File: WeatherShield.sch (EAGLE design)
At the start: 66 parts, among them J7 M023.5MM, J8 M023.5MM, Q1 BSS138, Q2 BSS138, U1 DS3231SN, U2 LT3652, U4 MPL3115A2LGA8, U5 HTU21D

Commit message: Power parts
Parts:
- removed J7, J8: M023.5MM, SparkFun-Connectors:M023.5MM
- removed L1: 68uH, SparkFun-Passives:INDUCTOR68UH-1A
- added L2: (no value), rcl:L-EU6000-XXX-RC
- C3, C4: device SparkFun-Capacitors:47UF-TANT -> FSEWeatherShield:47UF-16V-10%(TANT)
- R21, R23, R8: device rcl:R-EU_R0603 -> rcl:R-EU_R0805
- U$3: value DEAN_CONNECTOR -> V_BATT
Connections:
- net GND: no longer J8.2
- net N$14: no longer J7.2, J8.1
- net SENSE: now also L2.2; no longer L1.2
- net SFSASDF: no longer J7.1
- net SW: now also L2.1; no longer L1.1
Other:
- note added: "Ichg = .1/(R8) Add more Resitors parallel to increase Ichg"
- note added: "NB: DO NOT short JP1 & JP2 !! With both JP1 and JP2 shorted, the second power input is also shorted! This may result in damage to your power source."
- note removed: "01"
- note removed: "Ichg = .1/(R8) Add more Resitors in parallel to increase Ichg"
- note removed: "NB: With both JP1 and JP2 shorted, the second power input is also shorted! This may result in damage to your power source. You've been warned!"
- moved on the sheet: C9, D1, D3, JP1, JP10-DNP, JP2, JP9-DNP1, JP9-DNP2, R1, R15, R21, R23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

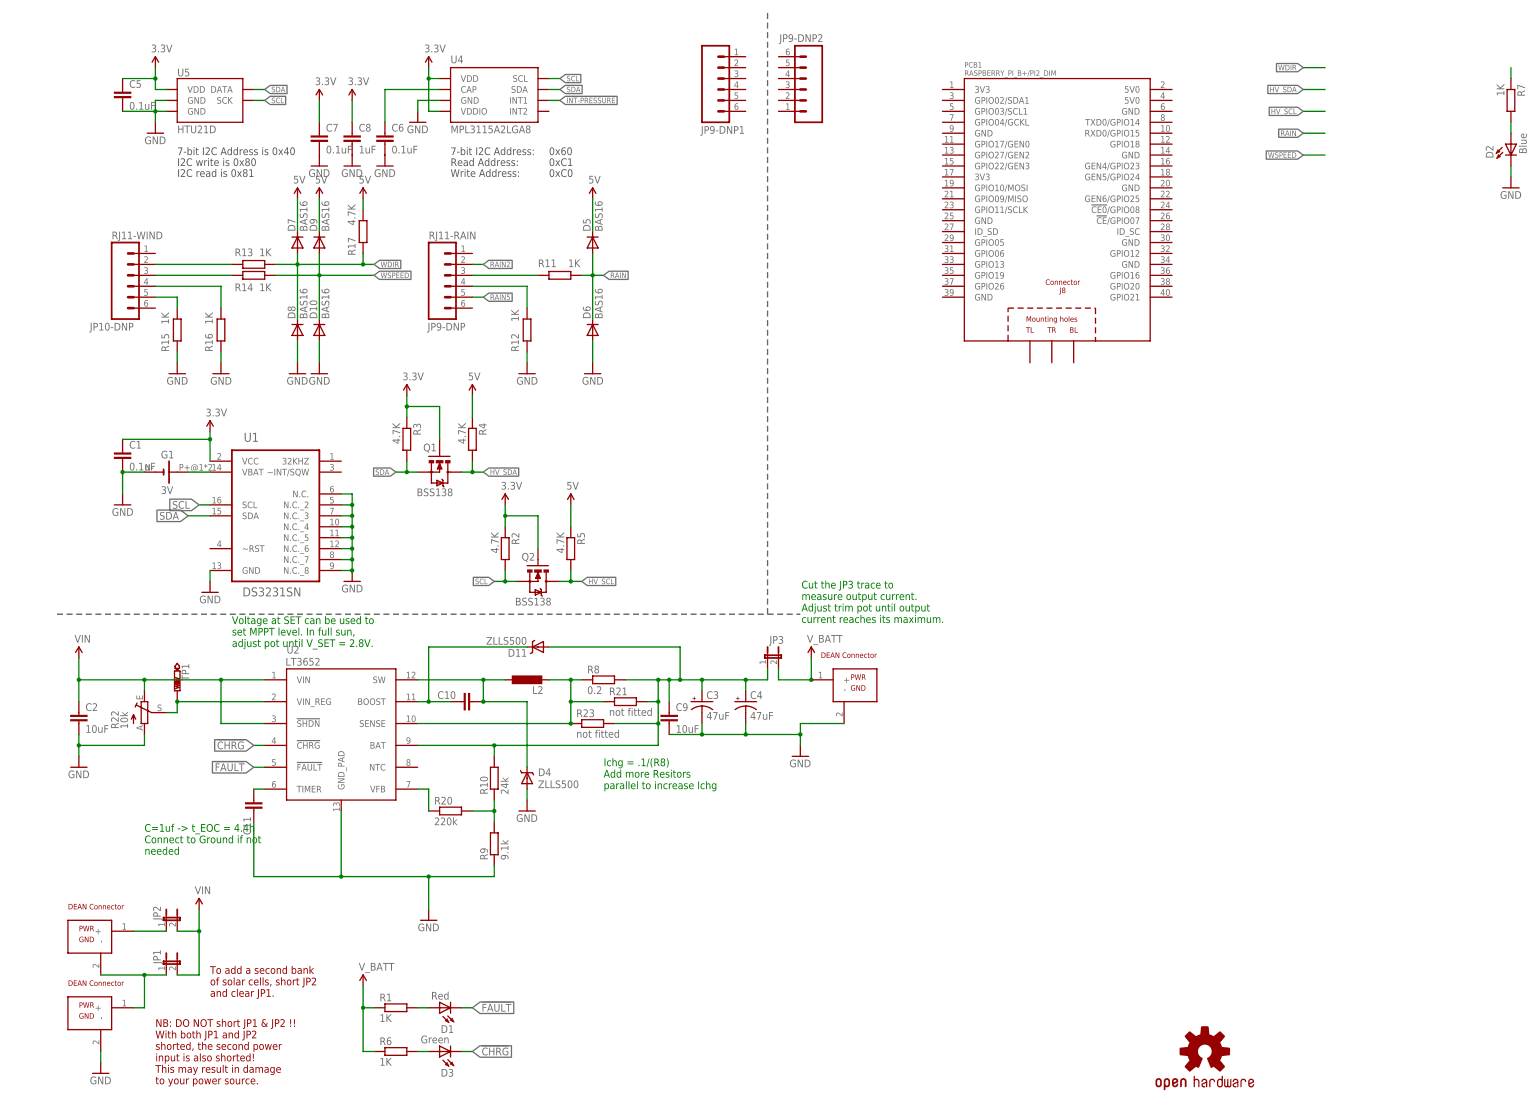
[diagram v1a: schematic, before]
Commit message: 5V supply done
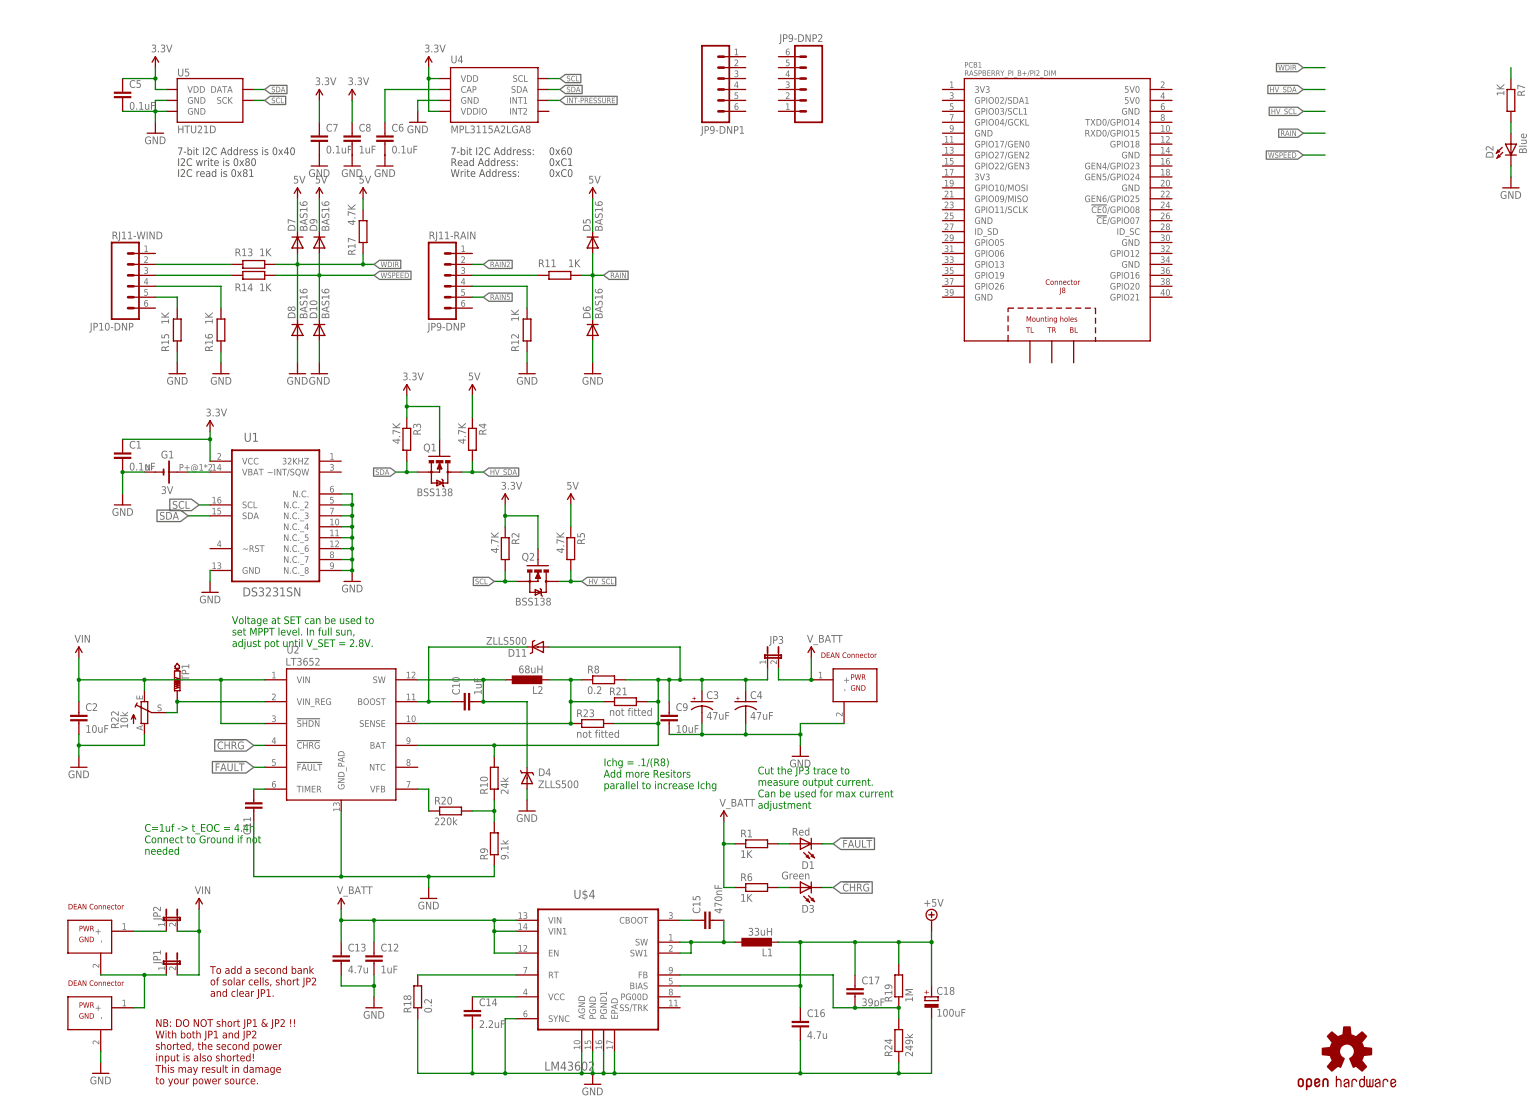
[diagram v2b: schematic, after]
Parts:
- added C12: 1uF, rcl:C-EUC0603
- added C13, C16: 4.7u, rcl:C-EUC0603
- added C14: 2.2uF, rcl:C-EUC0603
- added C15: 470nF, rcl:C-EUC0603
- added C17: 39pF, rcl:C-EUC0603
- added C18: 100uF, rcl:CPOL-EUE2,5-6E
- added L1: 33uH, rcl:L-EU6000-XXX-RC
- added R18: 0.2, rcl:R-EU_R0805
- added R19: 1M, rcl:R-EU_R0805
- added R24: 249k, rcl:R-EU_R0805
- added U$4: LM43602, FSEWeatherShield:LM43602
- C10: value 1.0uF -> 1uF
- L2: value (none) -> 68uH
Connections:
- new net +5V: C16.1, C17.1, C18.+, L1.2, R19.2, U$4.BIAS
- new net N$17: C15.1, U$4.CBOOT
- new net N$21: R18.2, U$4.RT
- new net N$22: C17.2, R19.1, R24.2, U$4.FB
- new net N$23: C14.1, U$4.VCC
- new net N$24: C15.2, L1.1, U$4.SW, U$4.SW1
- net GND: now also C12.2, C13.2, C14.2, C16.2, C18.-, R18.1, R24.1, U$4.AGND, U$4.EPAD, U$4.PGND, U$4.PGND1, U$4.SYNC
- net V_BATT: now also C12.1, C13.1, U$4.EN, U$4.VIN, U$4.VIN1
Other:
- note added: "Cut the JP3 trace to measure output current. Can be used for max current adjustment"
- note removed: "Cut the JP3 trace to measure output current. Adjust trim pot until output current reaches its maximum."
- moved on the sheet: D1, D3, R1, R6

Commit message: EagleCleanup.py added
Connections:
- new net N$18: JP9-DNP1.6, JP9-DNP2.1
- new net N$19: JP9-DNP1.5, JP9-DNP2.2
- new net N$20: JP9-DNP1.4, JP9-DNP2.3
- new net N$25: JP9-DNP1.3, JP9-DNP2.4
- new net N$26: JP9-DNP1.2, JP9-DNP2.5
- new net N$27: JP9-DNP1.1, JP9-DNP2.6
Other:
- moved on the sheet: JP9-DNP1, JP9-DNP2
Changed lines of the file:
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@@
 <instance part="G1" gate="G$1" x="30.48" y="149.86"/>
 <instance part="PCB1" gate="G$1" x="238.76" y="215.9"/>
-<instance part="JP9-DNP1" gate="G$1" x="160.02" y="241.3" smashed="yes" rot="MR180">
-<attribute name="NAME" x="154.686" y="228.473" size="1.778" layer="95"/>
-<attribute name="VALUE" x="154.94" y="251.46" size="1.778" layer="96" rot="MR180"/>
+<instance part="JP9-DNP1" gate="G$1" x="157.48" y="220.98" smashed="yes" rot="MR180">
+<attribute name="NAME" x="152.146" y="208.153" size="1.778" layer="95"/>
+<attribute name="VALUE" x="152.4" y="231.14" size="1.778" layer="96" rot="MR180"/>
 </instance>
-<instance part="JP9-DNP2" gate="G$1" x="177.8" y="238.76" smashed="yes" rot="MR0">
-<attribute name="NAME" x="183.134" y="251.587" size="1.778" layer="95" rot="R180"/>
-<attribute name="VALUE" x="182.88" y="228.6" size="1.778" layer="96" rot="MR0"/>
+<instance part="JP9-DNP2" gate="G$1" x="193.04" y="218.44" smashed="yes" rot="MR0">
+<attribute name="NAME" x="198.374" y="231.267" size="1.778" layer="95" rot="R180"/>
+<attribute name="VALUE" x="198.12" y="208.28" size="1.778" layer="96" rot="MR0"/>
 </instance>
 <instance part="R7" gate="G$1" x="342.9" y="236.22" rot="R270"/>
@@
 </segment>
 </net>
+<net name="N$18" class="0">
+<segment>
+<pinref part="JP9-DNP1" gate="G$1" pin="6"/>
+<pinref part="JP9-DNP2" gate="G$1" pin="1"/>
+<wire x1="187.96" y1="213.36" x2="162.56" y2="213.36" width="0.1524" layer="91"/>
+</segment>
+</net>
+<net name="N$19" class="0">
+<segment>
+<pinref part="JP9-DNP1" gate="G$1" pin="5"/>
+<pinref part="JP9-DNP2" gate="G$1" pin="2"/>
+<wire x1="187.96" y1="215.9" x2="162.56" y2="215.9" width="0.1524" layer="91"/>
+</segment>
+</net>
+<net name="N$20" class="0">
+<segment>
+<pinref part="JP9-DNP1" gate="G$1" pin="4"/>
+<pinref part="JP9-DNP2" gate="G$1" pin="3"/>
+<wire x1="187.96" y1="218.44" x2="162.56" y2="218.44" width="0.1524" layer="91"/>
+</segment>
+</net>
+<net name="N$25" class="0">
+<segment>
+<pinref part="JP9-DNP1" gate="G$1" pin="3"/>
+<pinref part="JP9-DNP2" gate="G$1" pin="4"/>
+<wire x1="187.96" y1="220.98" x2="162.56" y2="220.98" width="0.1524" layer="91"/>
+</segment>
+</net>
+<net name="N$26" class="0">
+<segment>
+<pinref part="JP9-DNP1" gate="G$1" pin="2"/>
+<pinref part="JP9-DNP2" gate="G$1" pin="5"/>
+<wire x1="187.96" y1="223.52" x2="162.56" y2="223.52" width="0.1524" layer="91"/>
+</segment>
+</net>
+<net name="N$27" class="0">
+<segment>
+<pinref part="JP9-DNP1" gate="G$1" pin="1"/>
+<pinref part="JP9-DNP2" gate="G$1" pin="6"/>
+<wire x1="187.96" y1="226.06" x2="162.56" y2="226.06" width="0.1524" layer="91"/>
+</segment>
+</net>

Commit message: Power parts
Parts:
- added D12: AirBoard status led, SparkFun:LED0603
- added R25: 1K, rcl:R-EU_R0603
- JP1: device SparkFun-Passives:JUMPER-2SMD-NC -> jumper:JP1E
- JP2: device SparkFun-Passives:JUMPER-2SMD-NO -> jumper:JP1E
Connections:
- new net N$28: D12.A, R25.2
- new net STAT1: R25.1
- net GND: now also D12.C
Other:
- moved on the sheet: D2, R7
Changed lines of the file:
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@@
 <part name="R9" library="rcl" deviceset="R-EU_" device="R0603" value="9.1k"/>
 <part name="R10" library="rcl" deviceset="R-EU_" device="R0603" value="24k"/>
-<part name="JP1" library="SparkFun-Passives" deviceset="JUMPER-2" device="SMD-NC"/>
+<part name="JP1" library="jumper" deviceset="JP1E" device=""/>
 <part name="GND20" library="SparkFun-Aesthetics" deviceset="GND" device=""/>
-<part name="JP2" library="SparkFun-Passives" deviceset="JUMPER-2" device="SMD-NO"/>
+<part name="JP2" library="jumper" deviceset="JP1E" device=""/>
 <part name="SUPPLY9" library="SparkFun-Aesthetics" deviceset="VIN" device=""/>
 <part name="SUPPLY11" library="SparkFun-Aesthetics" deviceset="V_BATT" device=""/>
@@
 <part name="C18" library="rcl" deviceset="CPOL-EU" device="E2,5-6E" value="100uF"/>
 <part name="SUPPLY12" library="supply2" deviceset="+5V" device=""/>
+<part name="R25" library="rcl" deviceset="R-EU_" device="R0603" value="1K"/>
+<part name="D12" library="SparkFun" deviceset="LED" device="0603" value="AirBoard status led"/>
+<part name="GND18" library="SparkFun" deviceset="GND" device=""/>
 </parts>
 <sheets>
@@
 <instance part="U1" gate="A" x="53.34" y="137.16"/>
 <instance part="GND1" gate="1" x="40.64" y="121.92" rot="MR0"/>
-<instance part="P+1" gate="1" x="40.64" y="159.258"/>
+<instance part="P+1" gate="1" x="40.64" y="164.338"/>
 <instance part="GND4" gate="1" x="73.66" y="124.46" rot="MR0"/>
 <instance part="C1" gate="G$1" x="20.32" y="154.94"/>
@@
 <attribute name="VALUE" x="198.12" y="208.28" size="1.778" layer="96" rot="MR0"/>
 </instance>
-<instance part="R7" gate="G$1" x="342.9" y="236.22" rot="R270"/>
-<instance part="D2" gate="G$1" x="342.9" y="226.06" smashed="yes">
-<attribute name="NAME" x="337.058" y="225.806" size="1.778" layer="95" rot="R270"/>
-<attribute name="VALUE" x="346.583" y="223.774" size="1.778" layer="96" rot="R90"/>
-</instance>
-<instance part="GND10" gate="1" x="342.9" y="215.9"/>
+<instance part="R7" gate="G$1" x="243.84" y="30.48" rot="R270"/>
+<instance part="D2" gate="G$1" x="243.84" y="20.32" smashed="yes">
+<attribute name="NAME" x="237.998" y="20.066" size="1.778" layer="95" rot="R270"/>
+<attribute name="VALUE" x="247.523" y="18.034" size="1.778" layer="96" rot="R90"/>
+</instance>
+<instance part="GND10" gate="1" x="243.84" y="10.16"/>
 <instance part="FRAME2" gate="G$1" x="0" y="0"/>
 <instance part="U2" gate="G$1" x="58.42" y="73.66"/>
@@
 <instance part="C18" gate="G$1" x="208.28" y="27.94"/>
 <instance part="SUPPLY12" gate="+5V" x="208.28" y="45.72"/>
+<instance part="R25" gate="G$1" x="231.14" y="30.48" rot="R270"/>
+<instance part="D12" gate="G$1" x="231.14" y="20.32" smashed="yes">
+<attribute name="NAME" x="225.298" y="20.066" size="1.778" layer="95" rot="R270"/>
+<attribute name="VALUE" x="234.823" y="7.874" size="1.778" layer="96" rot="R90"/>
+</instance>
+<instance part="GND18" gate="1" x="231.14" y="10.16"/>
 </instances>
 <busses>
@@
 </segment>
 <segment>
-<wire x1="342.9" y1="218.44" x2="342.9" y2="220.98" width="0.1524" layer="91"/>
+<wire x1="243.84" y1="12.7" x2="243.84" y2="15.24" width="0.1524" layer="91"/>
 <pinref part="D2" gate="G$1" pin="C"/>
 <pinref part="GND10" gate="1" pin="GND"/>
@@
 <junction x="78.74" y="30.48"/>
 </segment>
+<segment>
+<wire x1="231.14" y1="12.7" x2="231.14" y2="15.24" width="0.1524" layer="91"/>
+<pinref part="D12" gate="G$1" pin="C"/>
+<pinref part="GND18" gate="1" pin="GND"/>
+</segment>
 </net>
 <net name="N$7" class="0">
@@
 <pinref part="U1" gate="A" pin="VCC"/>
 <pinref part="P+1" gate="1" pin="VCC"/>
-<wire x1="40.64" y1="159.258" x2="40.64" y2="157.48" width="0.1524" layer="91"/>
+<wire x1="40.64" y1="164.338" x2="40.64" y2="157.48" width="0.1524" layer="91"/>
 <pinref part="C1" gate="G$1" pin="1"/>
 <wire x1="40.64" y1="157.48" x2="40.64" y2="152.4" width="0.1524" layer="91"/>
@@
 <net name="STAT3" class="0">
 <segment>
-<wire x1="342.9" y1="243.84" x2="342.9" y2="241.3" width="0.1524" layer="91"/>
+<wire x1="243.84" y1="38.1" x2="243.84" y2="35.56" width="0.1524" layer="91"/>
 <pinref part="R7" gate="G$1" pin="1"/>
 </segment>
@@
 <net name="N$10" class="0">
 <segment>
-<wire x1="342.9" y1="231.14" x2="342.9" y2="228.6" width="0.1524" layer="91"/>
+<wire x1="243.84" y1="25.4" x2="243.84" y2="22.86" width="0.1524" layer="91"/>
 <pinref part="R7" gate="G$1" pin="2"/>
 <pinref part="D2" gate="G$1" pin="A"/>
@@
 </segment>
 </net>
+<net name="STAT1" class="0">
+<segment>
+<wire x1="231.14" y1="38.1" x2="231.14" y2="35.56" width="0.1524" layer="91"/>
+<pinref part="R25" gate="G$1" pin="1"/>
+</segment>
+</net>
+<net name="N$28" class="0">
+<segment>
+<wire x1="231.14" y1="25.4" x2="231.14" y2="22.86" width="0.1524" layer="91"/>
+<pinref part="R25" gate="G$1" pin="2"/>
+<pinref part="D12" gate="G$1" pin="A"/>
+</segment>
+</net>

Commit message: routing
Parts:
- removed R18: 0.2, rcl:R-EU_R0805
- added C19: 0.1uF, rcl:C-EUC1206
- C12: value 1uF -> 0.1uF; device rcl:C-EUC0603 -> rcl:C-EUC1206
- C13: device rcl:C-EUC0603 -> rcl:C-EUC1206
- C17: value 39pF -> 47pF
- L1: value 33uH -> 10uH
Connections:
- removed net N$18: JP9-DNP1.6, JP9-DNP2.1
- removed net N$19: JP9-DNP1.5, JP9-DNP2.2
- removed net N$20: JP9-DNP1.4, JP9-DNP2.3
- removed net N$21: R18.2, U$4.RT
- removed net N$25: JP9-DNP1.3, JP9-DNP2.4
- removed net N$26: JP9-DNP1.2, JP9-DNP2.5
- removed net N$27: JP9-DNP1.1, JP9-DNP2.6
- net +5V: now also C19.1
- net 5V: now also PCB1.5V0@1, PCB1.5V0@2
- net GND: now also C19.2, PCB1.GND@1, PCB1.GND@2, PCB1.GND@3, PCB1.GND@4, PCB1.GND@5, PCB1.GND@6, PCB1.GND@7, PCB1.GND@8; no longer R18.1
- net VCC: now also PCB1.3V3@1, PCB1.3V3@2
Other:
- moved on the sheet: JP9-DNP1, JP9-DNP2

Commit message: Power parts
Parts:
- added C20, C21: 0.1uF, rcl:C-EUC0603
- added U$5: MCP3221A5T-E/OT, FSEWeatherShield:MCP3221A5T-E/OT
- JP10-DNP, JP9-DNP: device SparkFun:RJ11-6PTH -> FSEWeatherShield:RJ11-BUCHSE
- JP9-DNP1, JP9-DNP2: value RJ11-6PTH -> RJ11-BUCHSE; device SparkFun:RJ11-6PTH -> FSEWeatherShield:RJ11-BUCHSE
- R22: value 10k -> (none); device pot:TRIM_EU-S64Y -> pot:TRIM_EU-SM-42/43A
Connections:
- net 5V: now also C20.1, C21.1, U$5.VDD
- net GND: now also C20.2, C21.2, U$5.VSS
- net SCL: now also U$5.SCL
- net SDA: now also U$5.SDA
- net WDIR: now also U$5.AIN
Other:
- moved on the sheet: C5, C6, C7, C8, D10, D5, D6, D7, D8, D9, Q1, Q2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

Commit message: Power parts
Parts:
- removed JP1, JP2: (no value), jumper:JP1E
- removed U$1: DEAN_CONNECTOR, FSE_Weather_Shield:DEAN_CONNECTOR
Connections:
- removed net N$14: JP1.1, U$1.-, U$2.+
- removed net SFSASDF: JP2.1, U$1.+
- net 5V: now also JP9-DNP1.1, JP9-DNP2.1
- net GND: now also JP9-DNP1.5, JP9-DNP1.6, JP9-DNP2.5, JP9-DNP2.6
- net SCL: now also JP9-DNP1.4, JP9-DNP2.4
- net SDA: now also JP9-DNP1.3, JP9-DNP2.3
- net VCC: now also JP9-DNP1.2, JP9-DNP2.2
- net VIN: now also U$2.+; no longer JP1.2, JP2.2
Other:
- note removed: "NB: DO NOT short JP1 & JP2 !! With both JP1 and JP2 shorted, the second power input is also shorted! This may result in damage to your power source."
- note removed: "To add a second bank of solar cells, short JP2 and clear JP1."
- moved on the sheet: D1, D3, JP9-DNP1, R1, R6

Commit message: WeatherShield_v1
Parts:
- removed U$2: DEAN_CONNECTOR, FSE_Weather_Shield:DEAN_CONNECTOR
- removed U$3: V_BATT, FSE_Weather_Shield:DEAN_CONNECTOR
- added U$1, U$6: XT-60, FSEWeatherShield:XT-60
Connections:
- removed net +5V: C16.1, C17.1, C18.+, C19.1, L1.2, R19.2, U$4.BIAS
- removed net VCC: C1.1, JP9-DNP1.2, JP9-DNP2.2, PCB1.3V3@1, PCB1.3V3@2, U1.VCC
- net 3.3V: now also C1.1, JP9-DNP1.2, JP9-DNP2.2, PCB1.3V3@1, PCB1.3V3@2, U1.VCC
- net 5V: now also C16.1, C17.1, C18.+, C19.1, L1.2, R19.2, U$4.BIAS
- net GND: now also U$1.-, U$6.-; no longer U$2.-, U$3.-
- net VIN: now also U$1.+; no longer U$2.+
- net V_BATT: now also U$6.+; no longer U$3.+
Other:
- moved on the sheet: C2, C20, C21, R22, U$5
